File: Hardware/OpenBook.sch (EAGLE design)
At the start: 103 parts, among them IC1 BD5229G-TR, IC4 XC6220A331MR-G, J1 FH34SRJ-24S-0.5SH_99_, J2 SAMACSYS_PARTS_USB4110-GF-A, J3 QWIIC_RIGHT_ANGLE, J4 112A-TAAR-R03_ATTEND, Q1 20V/4.2A/52mΩ/1.4W, Q2 20V/4.2A/52mΩ/1.4W, Q3 SI1308EDL-T1-GE3, U1 W25Q512JVEIQ, U2 ESP32-C6-WROOM-1-N8, U3 DS3231SN#, U4 MAX17048G+T10

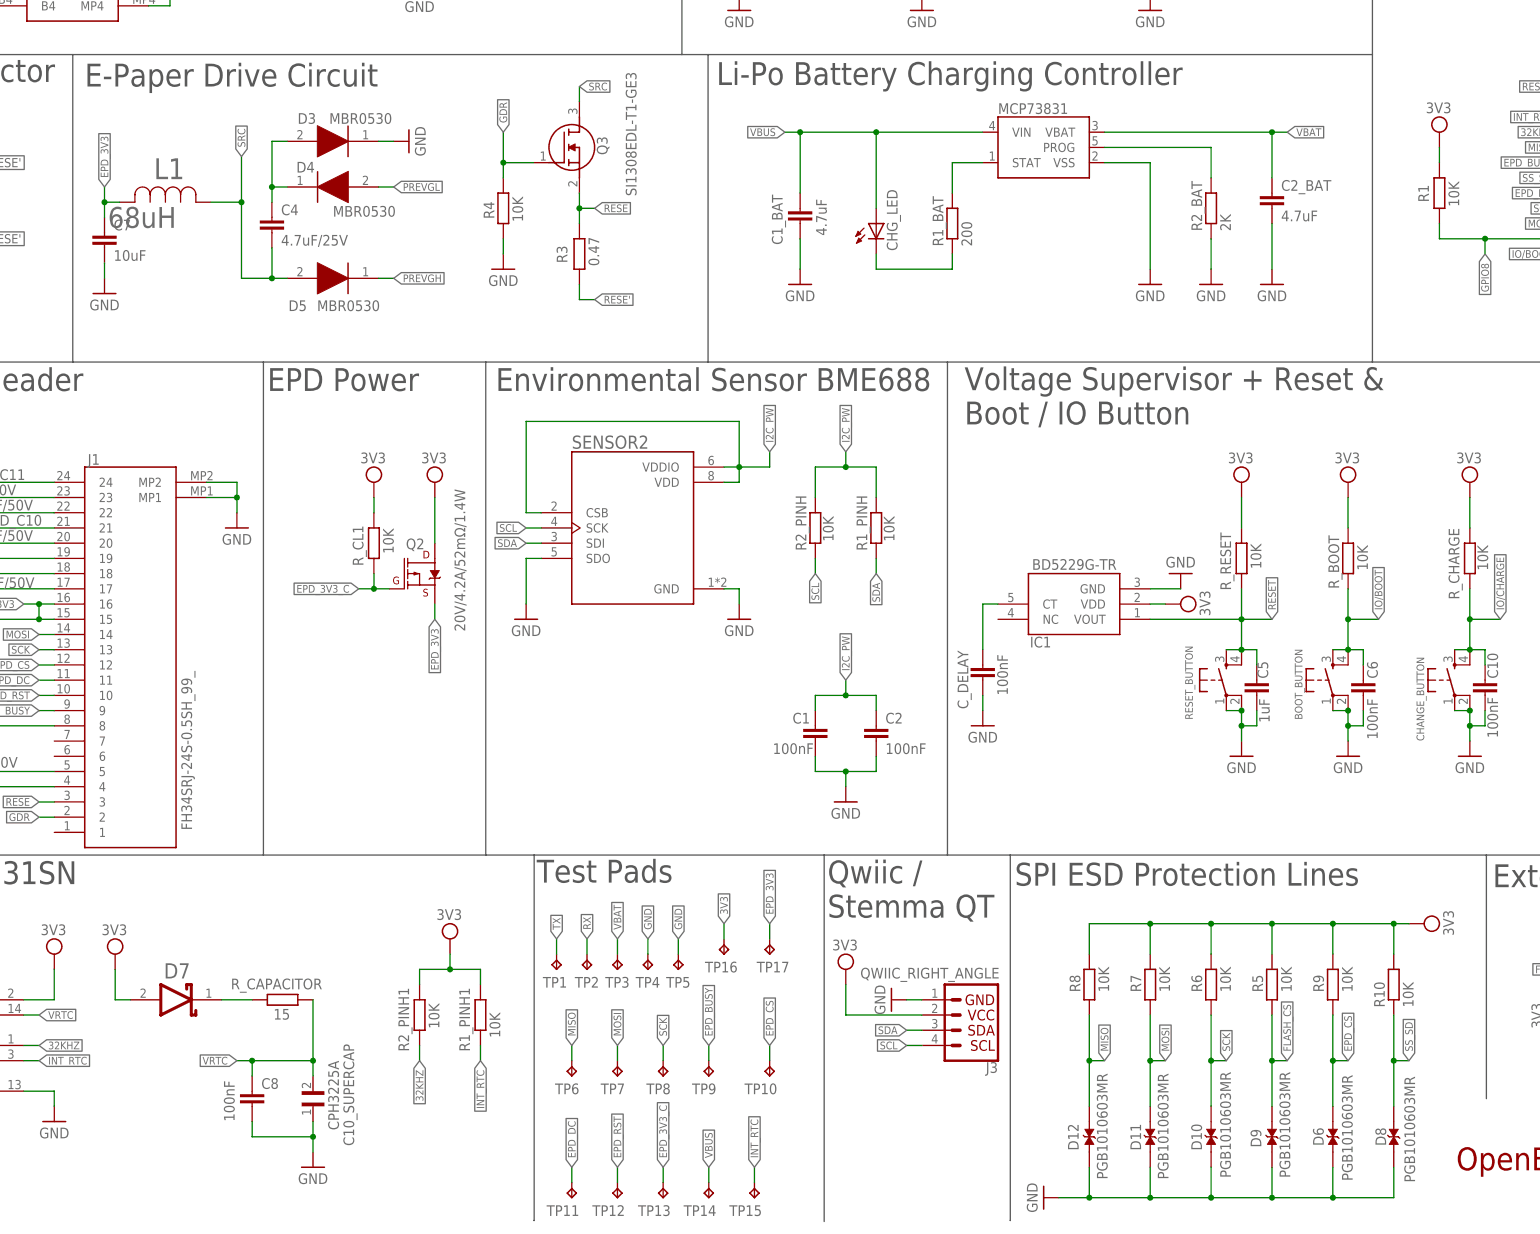
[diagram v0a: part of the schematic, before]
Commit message: added 3d models for components; added render images
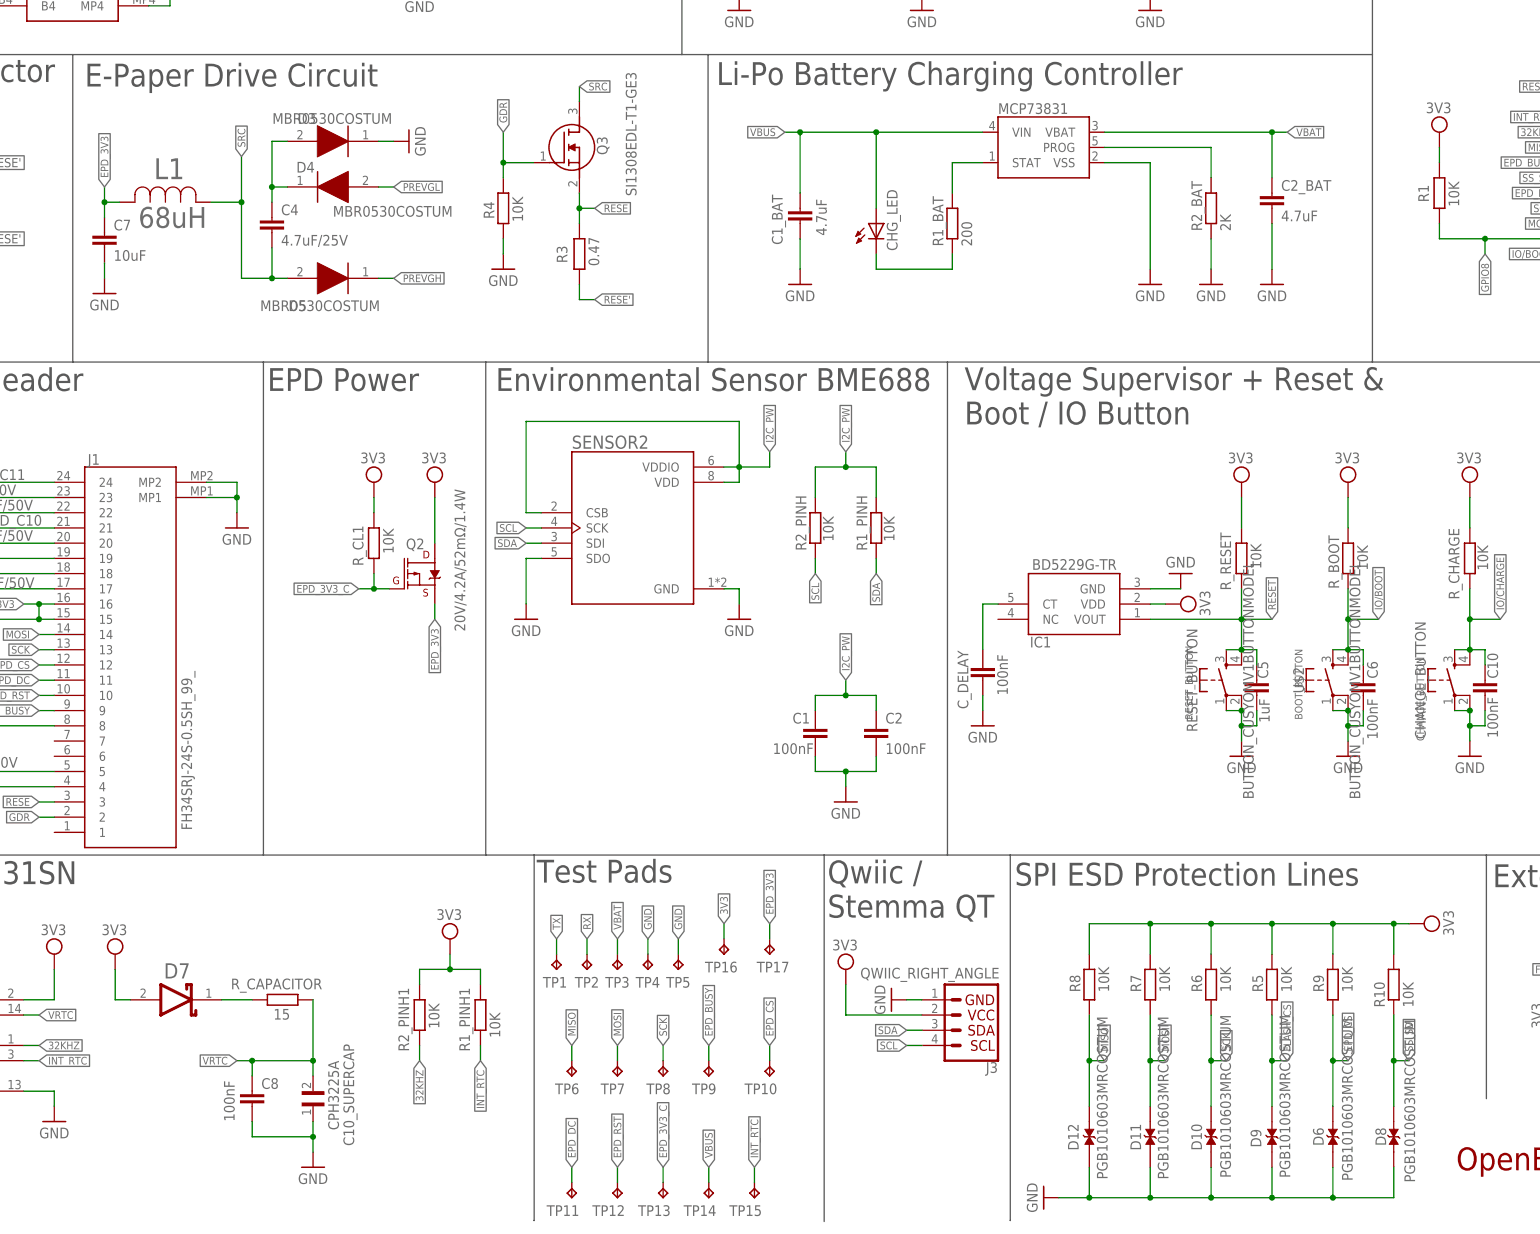
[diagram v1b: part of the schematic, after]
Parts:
- C1, C10, C1_BAT, C1_BAT1, C1_BAT2, C2, C2_BAT, C4, C4_USB, C5, C5_USB, C6, C7, C8, C9, C_DELAY, EPD_C1, EPD_C10, EPD_C11, EPD_C12, EPD_C2, EPD_C5, EPD_C6, EPD_C7, EPD_C8, EPD_C9: device DeskAssistant v19 v1:ESP32_WROVER_EAGLE-LTSPICE_CC0402 -> DeskAssistant v19 v1:ESP32_WROVER_EAGLE-LTSPICE_C
- CHANGE_BUTTON, RESET_BUTTON, U$2: value BUTTON_CUSYOMV1 -> BUTTON_CUSYOMV1BUTTONMODEL; device DeskAssistant v19 v1:BUTTON_CUSYOMV1 -> DeskAssistant v19 v1:BUTTON_CUSYOMV1BUTTONMODEL
- D10, D11, D12, D6, D8, D9: value PGB1010603MR -> PGB1010603MRCOSTUM; device DeskAssistant v19 v1:PGB1010603MR -> DeskAssistant v19 v1:PGB1010603MRCOSTUM
- D3, D4, D5: value MBR0530 -> MBR0530COSTUM; device DeskAssistant v19 v1:MBR0530 -> DeskAssistant v19 v1:MBR0530COSTUM
- R1, R10, R1_BAT, R1_PINH, R1_PINH1, R1_PWRUSB, R2, R2-USB, R2-USB1, R2_BAT, R2_PINH, R2_PINH1, R3, R4, R5, R6, R7, R8, R9, R_BOOT, R_CAPACITOR, R_CHARGE, R_CL1, R_RESET: device DeskAssistant v19 v1:ESP32_WROVER_EAGLE-LTSPICE_RR0402 -> DeskAssistant v19 v1:ESP32_WROVER_EAGLE-LTSPICE_R
- TP1, TP10, TP11, TP12, TP13, TP14, TP15, TP16, TP17, TP2, TP3, TP4, TP5, TP6, TP7, TP8, TP9: value TPTP20R -> TP; device DeskAssistant v19 v1:TPTP20R -> DeskAssistant v19 v1:TP
